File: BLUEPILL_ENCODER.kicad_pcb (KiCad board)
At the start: 2 copper layers, 34 parts, among them J1 Conn_01x03, J2 Conn_01x04, J3 USB_C_Receptacle_USB2.0_16P, J4 Conn_01x08, SW1 SW_SPDT, U1 STM32F103C8T6, U2 AMS1117-3.3, U4 AS5600L-ASOM, Y2 8Mz

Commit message: Add files via upload
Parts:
- C1, C12, C13, C2, C3, C4, C7, C8: footprint Capacitor_SMD:C_0603_1608Metric_Pad1.08x0.95mm_HandSolder -> Capacitor_Tantalum_SMD:CP_EIA-3528-21_Kemet-B_HandSolder; moved to B.Cu
- C10, C11, C9: footprint Capacitor_SMD:C_0603_1608Metric_Pad1.08x0.95mm_HandSolder -> Capacitor_Tantalum_SMD:CP_EIA-3528-21_Kemet-B_HandSolder
- C5, C6, FB1, R1, R3, R5, R6, R7, R8, U2, U4: moved to B.Cu
- J1: value Conn_01x03 -> boot
- J2: footprint Connector_PinHeader_2.54mm:PinHeader_1x04_P2.54mm_Horizontal -> Connector_PinHeader_2.54mm:PinHeader_1x04_P2.54mm_Vertical
- J3: footprint Connector_USB:USB_C_Receptacle_GCT_USB4085 -> Connector_USB:USB_C_Receptacle_GCT_USB4105-xx-A_16P_TopMnt_Horizontal
- R2: value 330 -> 10k; moved to B.Cu
- SW1: value SW_SPDT -> RESET_SWITCH; footprint Button_Switch_SMD:SW_SPST_EVQP2_MiddlePushTravel_H2.5mm -> TS09-stm32_reset_original_button:SW_TS09-63-25-R-260-SMT-TR
- Y2: footprint Crystal:Crystal_SMD_5032-2Pin_5.0x3.2mm_HandSoldering -> ABM3-8.000MHZ-D2Y-T__ABRACON_8MHz_crystral:XTAL_ABM3-8.000MHZ-D2Y-T
- moved R7 104.7 mm to (188.9, 60.6), turned to 180 degrees
- moved R4 103.9 mm to (188.2, 78.5), turned to -90 degrees
- moved FB1 100.6 mm to (183.3, 47.3)
- moved R5 98.6 mm to (183.4, 77.0), turned to -90 degrees
- moved C7 98.5 mm to (187.5, 47.2), turned to 180 degrees
- moved J2 97.7 mm to (191.4, 69.3), turned to 180 degrees
- moved C12 96.8 mm to (191.2, 48.3), turned to -90 degrees
- moved R8 95.3 mm to (180.5, 77.0), turned to -90 degrees
- moved R3 92.8 mm to (177.9, 61.3), turned to 90 degrees
- moved C3 92.7 mm to (186.3, 62.7), turned to -90 degrees
- moved C1 91.6 mm to (185.8, 70.0), turned to -90 degrees
- moved R9 90.4 mm to (175.5, 78.7), turned to -90 degrees
- moved R2 89.7 mm to (174.8, 62.8)
- moved C2 88.4 mm to (182.5, 65.8)
- moved U4 86.6 mm to (181.4, 69.9), turned to 180 degrees
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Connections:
- R2 pad 2: Net-(SW1-A) -> NRST
- SW1 pad 1: Net-(SW1-A) -> NRST
- SW1 pad 2: NRST -> GND
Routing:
- net 3.3V_MAIN_POWER_RAIL: track 0.00 -> 79.9 mm, vias 0 -> 7
- net 5V_MAIN_INPUT_USB: track 0.00 -> 46.6 mm, vias 0 -> 3
- net NRST: track 0.00 -> 37.5 mm, vias 0 -> 2
- net SENSOR_ANLG_OUT: track 0.00 -> 28.5 mm, vias 0 -> 5
- net USART1_RX: track 0.00 -> 25.0 mm, vias 0 -> 5
- net BOOT0: track 0.00 -> 22.8 mm
- net GND: track 0.00 -> 22.7 mm, vias 0 -> 6
- net I2C_SCL: track 0.00 -> 17.0 mm, vias 0 -> 2
- net USART1_TX: track 0.00 -> 16.5 mm, vias 0 -> 1
- net USB_D+: track 0.00 -> 15.4 mm
- net I2C2_SDA: track 0.00 -> 15.4 mm, vias 0 -> 1
- net HSE_IN: track 0.00 -> 14.4 mm
- net TIM2_CH2: track 0.00 -> 13.5 mm, vias 0 -> 1
- net HSE_OUT: track 0.00 -> 13.0 mm
- net I2C2_SCL: track 0.00 -> 12.8 mm, vias 0 -> 1
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- added copper zone on B.Cu, net GND
- added copper zone on F.Cu, net GND
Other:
- board outline added: 24.4 x 21.4 mm
- board text added: "PCB Edge"

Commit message: Add files via upload
Pcb is ready, free from critical errors
Ready for manufacturing
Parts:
- removed C12, C13: 1u, Capacitor_Tantalum_SMD:CP_EIA-3528-21_Kemet-B_HandSolder
- removed C7, C8: 100n, Capacitor_Tantalum_SMD:CP_EIA-3528-21_Kemet-B_HandSolder
- removed FB1: 120R, FERRITE_BEAD:BEADC2012X105N
- C1, C10, C11, C2, C3, C4, C5, C6, C9: footprint Capacitor_Tantalum_SMD:CP_EIA-3528-21_Kemet-B_HandSolder -> Capacitor_SMD:C_0603_1608Metric_Pad1.08x0.95mm_HandSolder
- R2, R6: moved to F.Cu
- R9: moved to B.Cu
- moved D1 49.4 mm to (188.0, 71.2), turned to 180 degrees
- moved D2 41.2 mm to (175.7, 78.3), turned to 90 degrees
- moved R6 36.4 mm to (173.8, 78.3), turned to 90 degrees
- moved C5 33.3 mm to (174.4, 60.4), turned to 0 degrees
- moved R1 23.7 mm to (181.1, 60.6)
- moved R2 17.7 mm to (188.2, 74.3), turned to -90 degrees
- moved R9 1.60 mm to (173.9, 78.4)
- moved C2 0.89 mm to (182.8, 64.9), turned to 180 degrees
- moved C3 0.32 mm to (186.2, 63.0)
- moved R7 0.31 mm to (189.1, 60.4)
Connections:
- U1 pad 9: 3.3v_VDDA_FILTERED -> 3.3V_MAIN_POWER_RAIL
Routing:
- net GND: track 22.7 -> 82.5 mm, vias 6 -> 13
- net Net-(D1-A): track 0.00 -> 31.0 mm, vias 0 -> 3
- net I2C_SDA: track 10.7 -> 23.7 mm
- net 3.3V_MAIN_POWER_RAIL: track 79.9 -> 89.5 mm, vias 7 -> 8
- net HSE_OUT: track 13.0 -> 18.2 mm, vias 0 -> 2
- net 5V_MAIN_INPUT_USB: track 46.6 -> 50.7 mm, vias 3 -> 2
- net LED_BINK: track 0.00 -> 3.64 mm, vias 0 -> 1
- net SENSOR_ANLG_OUT: track 28.5 -> 32.0 mm, vias 5 -> 4
- net Net-(D2-A): track 0.00 -> 2.70 mm, vias 0 -> 1
- net HSE_IN: track 14.4 -> 16.7 mm
- net I2C_SCL: track 17.0 -> 18.6 mm
- net I2C2_SDA: track 15.4 -> 16.1 mm
- net NRST: track 37.5 -> 38.1 mm
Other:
- board size 24.4 x 21.4 mm -> 24.4 x 22 mm

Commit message: Add files via upload
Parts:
- renumbered D1 to PC13
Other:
- board text added: "PC13"
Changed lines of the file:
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@@
 			(at 0 -2.38 0)
 			(layer "F.SilkS")
+			(hide yes)
 			(effects
 				(font
@@
 			(at 0 -1.43 270)
 			(layer "F.SilkS")
+			(hide yes)
 			(effects
 				(font
@@
 		(descr "LED SMD 0603 (1608 Metric), square (rectangular) end terminal, IPC-7351 nominal, (Body size source: http://www.tortai-tech.com/upload/download/2011102023233369053.pdf), generated with kicad-footprint-generator")
 		(tags "LED handsolder")
-		(property "Reference" "D1"
-			(at 0 -1.43 0)
+		(property "Reference" "PC13"
+			(at 0 -0.53 0)
 			(layer "F.SilkS")
+			(hide yes)
 			(effects
 				(font
-					(size 1 1)
-					(thickness 0.15)
+					(size 0.2 0.2)
+					(thickness 0.05)
+					(bold yes)
 				)
 			)
@@
 			(layer "F.Fab")
 		)
-		(fp_text user "${REFERENCE}"
-			(at 0 0 0)
-			(layer "F.Fab")
-			(effects
-				(font
-					(size 0.4 0.4)
-					(thickness 0.06)
-				)
-			)
-		)
 		(pad "1" smd roundrect
 			(at -0.875 0 180)
@@
 			(at 14.64 -0.32 0)
 			(layer "F.Fab")
+			(hide yes)
 			(effects
 				(font
@@
 			(layer "F.Fab")
 		)
-		(fp_text user "${REFERENCE}"
-			(at 11.5 -1.37 90)
-			(layer "F.Fab")
-			(effects
-				(font
-					(size 1 1)
-					(thickness 0.15)
-				)
-			)
-		)
 		(pad "1" thru_hole rect
 			(at 0 0 180)
@@
 			(at 0 -1.43 270)
 			(layer "F.SilkS")
+			(hide yes)
 			(effects
 				(font
@@
 			(at 0 -1.65 90)
 			(layer "F.SilkS")
+			(hide yes)
 			(effects
 				(font
@@
 			(at 0 -2.38 0)
 			(layer "F.SilkS")
+			(hide yes)
 			(effects
 				(font
@@
 			(at 0 -1.43 90)
 			(layer "F.SilkS")
+			(hide yes)
 			(effects
 				(font
@@
 			(at 0 -1.43 270)
 			(layer "F.SilkS")
+			(hide yes)
 			(effects
 				(font
@@
 			(at 0 -1.65 90)
 			(layer "F.SilkS")
+			(hide yes)
 			(effects
 				(font
@@
 			(at 0 -1.65 90)
 			(layer "F.SilkS")
+			(hide yes)
 			(effects
 				(font
@@
 			(at 0 1.65 90)
 			(layer "B.SilkS")
+			(hide yes)
 			(effects
 				(font
@@
 			(at 0 1.65 90)
 			(layer "B.SilkS")
+			(hide yes)
 			(effects
 				(font
@@
 			(at 0 1.65 0)
 			(layer "B.SilkS")
+			(hide yes)
 			(effects
 				(font
@@
 			(at 0 1.65 90)
 			(layer "B.SilkS")
+			(hide yes)
 			(effects
 				(font
@@
 			(at 0 1.43 0)
 			(layer "B.SilkS")
+			(hide yes)
 			(effects
 				(font
@@
 			(at 0 1.43 0)
 			(layer "B.SilkS")
+			(hide yes)
 			(effects
 				(font
@@
 			(unlocked yes)
 			(layer "B.SilkS")
+			(hide yes)
 			(effects
 				(font
@@
 			(at 0 1.43 90)
 			(layer "B.SilkS")
+			(hide yes)
 			(effects
 				(font
@@
 			(at 0 1.43 90)
 			(layer "B.SilkS")
+			(hide yes)
 			(effects
 				(font
@@
 			(at 0 1.65 0)
 			(layer "B.SilkS")
+			(hide yes)
 			(effects
 				(font
@@
 			(at 0 1.43 90)
 			(layer "B.SilkS")
+			(hide yes)
 			(effects
 				(font
@@
 			(at 0 1.43 270)
 			(layer "B.SilkS")
+			(hide yes)
 			(effects
 				(font
@@
 			(at 0 1.65 90)
 			(layer "B.SilkS")
+			(hide yes)
 			(effects
 				(font
@@
 		(layer "Edge.Cuts")
 	)
+	(gr_text "PC13"
+		(at 187.96 71.8 0)
+		(layer "F.SilkS")
+		(effects
+			(font
+				(size 0.2 0.2)
+				(thickness 0.05)
+				(bold yes)
+			)
+		)
+	)
 	(gr_text "PCB Edge"
 		(at 181.7678 80.095 0)
@@
 		(polygon
 			(pts
-				(xy 166.7378 52.125) (xy 196.6678 52.125) (xy 196.6678 82.055) (xy 166.7378 82.055)
+				(xy 166.6278 56.795) (xy 196.5578 56.795) (xy 196.6678 82.055) (xy 166.7378 82.055)
 			)
 		)
@@
 		(polygon
 			(pts
-				(xy 166.7478 52.125) (xy 196.6478 52.105) (xy 196.6578 82.045) (xy 166.7378 82.035)
+				(xy 166.6378 57.275) (xy 196.5378 57.255) (xy 196.6578 82.045) (xy 166.7378 82.035)
 			)
 		)

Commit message: Add files via upload
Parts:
- removed PC13: LED, LED_SMD:LED_0603_1608Metric_Pad1.05x0.95mm_HandSolder
- added D1: LED, LED_SMD:LED_0603_1608Metric_Pad1.05x0.95mm_HandSolder, F.Cu at (188.0, 71.3)
- added REF**: MountingHole_2.1mm, MountingHole:MountingHole_2.1mm, F.Cu at (166.4, 54.7)
- added REF**: MountingHole_2.1mm, MountingHole:MountingHole_2.1mm, F.Cu at (196.4, 84.7)
- R1, R2, R3, R4, R5, R6, R7, R8, R9: footprint Resistor_SMD:R_0805_2012Metric_Pad1.20x1.40mm_HandSolder -> Resistor_SMD:R_0603_1608Metric_Pad0.98x0.95mm_HandSolder
- U4: footprint AS5600:SOIC8_AS5600_OSR -> ul_AS5600L-ASOM:AS5600L-ASOM_AMS
- moved C3 1.98 mm to (187.6, 64.4)
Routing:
- net GND: track 82.5 -> 94.7 mm, vias 13 -> 16
- net HSE_IN: track 16.7 -> 14.1 mm
- net I2C_SCL: track 18.6 -> 16.6 mm
- net 3.3V_MAIN_POWER_RAIL: track 89.5 -> 87.6 mm
- net LED_BINK: track 3.64 -> 5.23 mm
- net SENSOR_ANLG_OUT: track 32.0 -> 30.4 mm
- net HSE_OUT: track 18.2 -> 17.3 mm
- net BOOT1: track 4.33 -> 5.14 mm
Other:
- board size 24.4 x 22 mm -> 37.8 x 37.8 mm

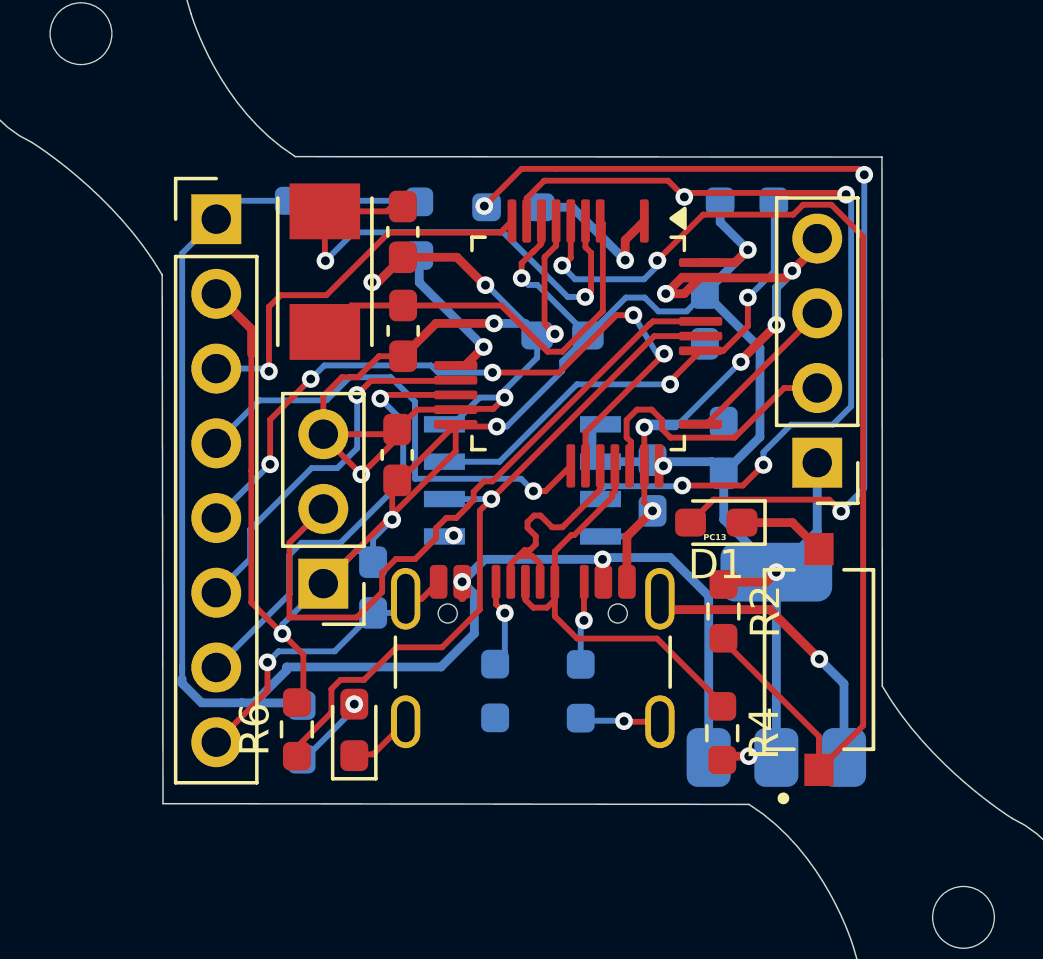
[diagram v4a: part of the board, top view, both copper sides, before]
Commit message: Add files via upload
SIGNIFICANTLY REDUCED TRACE LENGTH OF I2C PULL-UPs 
AND ERRORS RECTIFIED
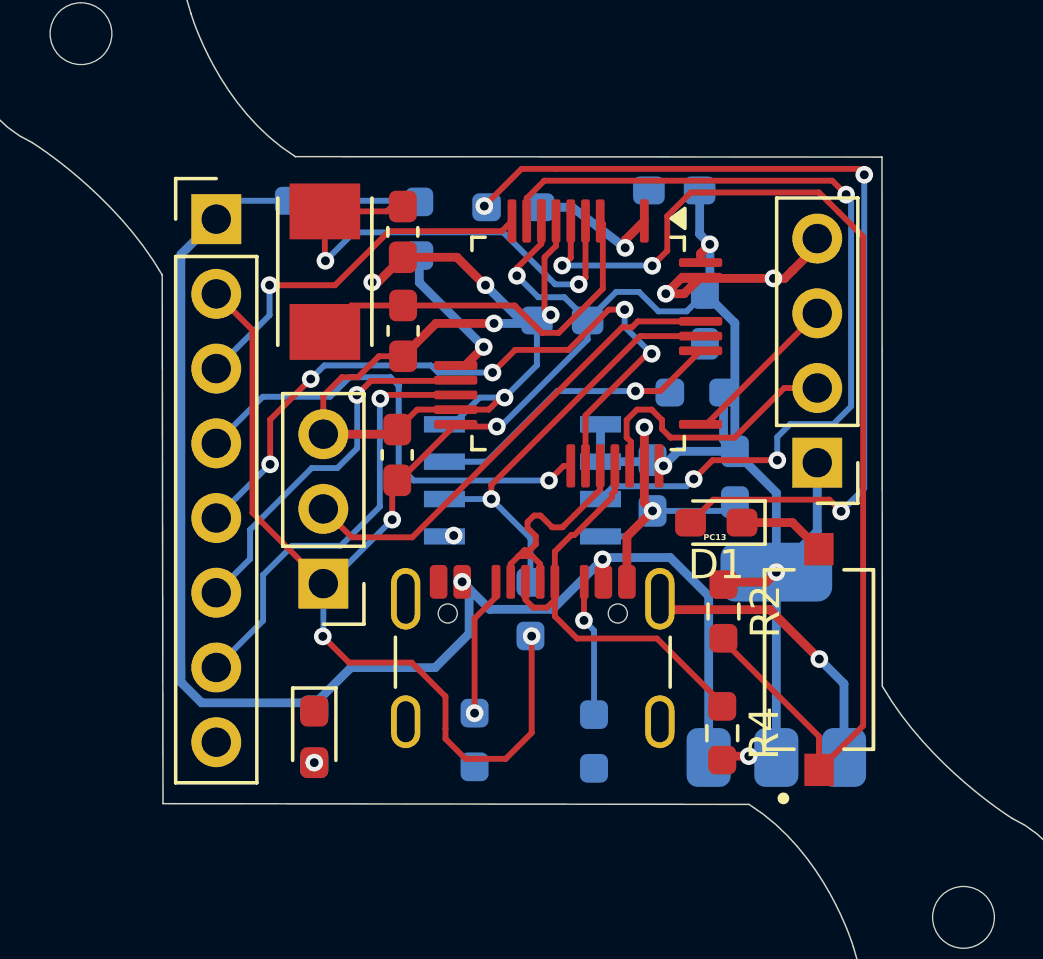
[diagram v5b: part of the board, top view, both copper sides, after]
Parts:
- R6: moved to B.Cu
- moved C4 16.9 mm to (186.6, 60.0), turned to 180 degrees
- moved R6 8.93 mm to (181.7, 74.2), turned to -90 degrees
- moved R7 6.72 mm to (187.3, 66.9), turned to 0 degrees
- moved R8 1.81 mm to (179.8, 78.7)
- moved R5 1.76 mm to (183.8, 78.7)
- moved D2 1.38 mm to (174.3, 78.6), turned to -90 degrees
- moved C6 1.05 mm to (188.6, 69.7), turned to -90 degrees
- moved C2 0.51 mm to (182.8, 64.4)
- moved R9 0.46 mm to (174.3, 78.6)
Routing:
- net GND: track 94.7 -> 67.0 mm, vias 16 -> 11
- net I2C_SDA: track 23.7 -> 14.4 mm
- net BOOT0: track 23.1 -> 16.3 mm
- net I2C_SCL: track 16.6 -> 11.5 mm, vias 2 -> 1
- net Net-(D2-A): track 2.70 -> 0.00 mm
- net Net-(J3-CC2): track 2.77 -> 4.81 mm
- net Net-(J3-CC1): track 3.03 -> 4.82 mm
- net 5V_MAIN_INPUT_USB: track 50.7 -> 49.2 mm
- net 3.3V_MAIN_POWER_RAIL: track 87.6 -> 88.8 mm, vias 8 -> 9
- net HSE_IN: track 14.1 -> 13.2 mm
- net HSE_OUT: track 17.3 -> 16.4 mm
- net TIM2_CH2: track 13.5 -> 12.7 mm
- net LED_BINK: track 5.23 -> 4.54 mm
- net SENSOR_ANLG_OUT: track 30.4 -> 30.2 mm, vias 4 -> 3

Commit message: Add files via upload
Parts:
- moved C11 0.18 mm to (177.2, 69.2)
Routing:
- net GND: track 67.0 -> 71.4 mm
- net Net-(D1-A): track 30.9 -> 33.3 mm
- net USART1_TX: track 16.2 -> 17.3 mm
